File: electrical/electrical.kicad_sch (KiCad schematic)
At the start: 0 parts

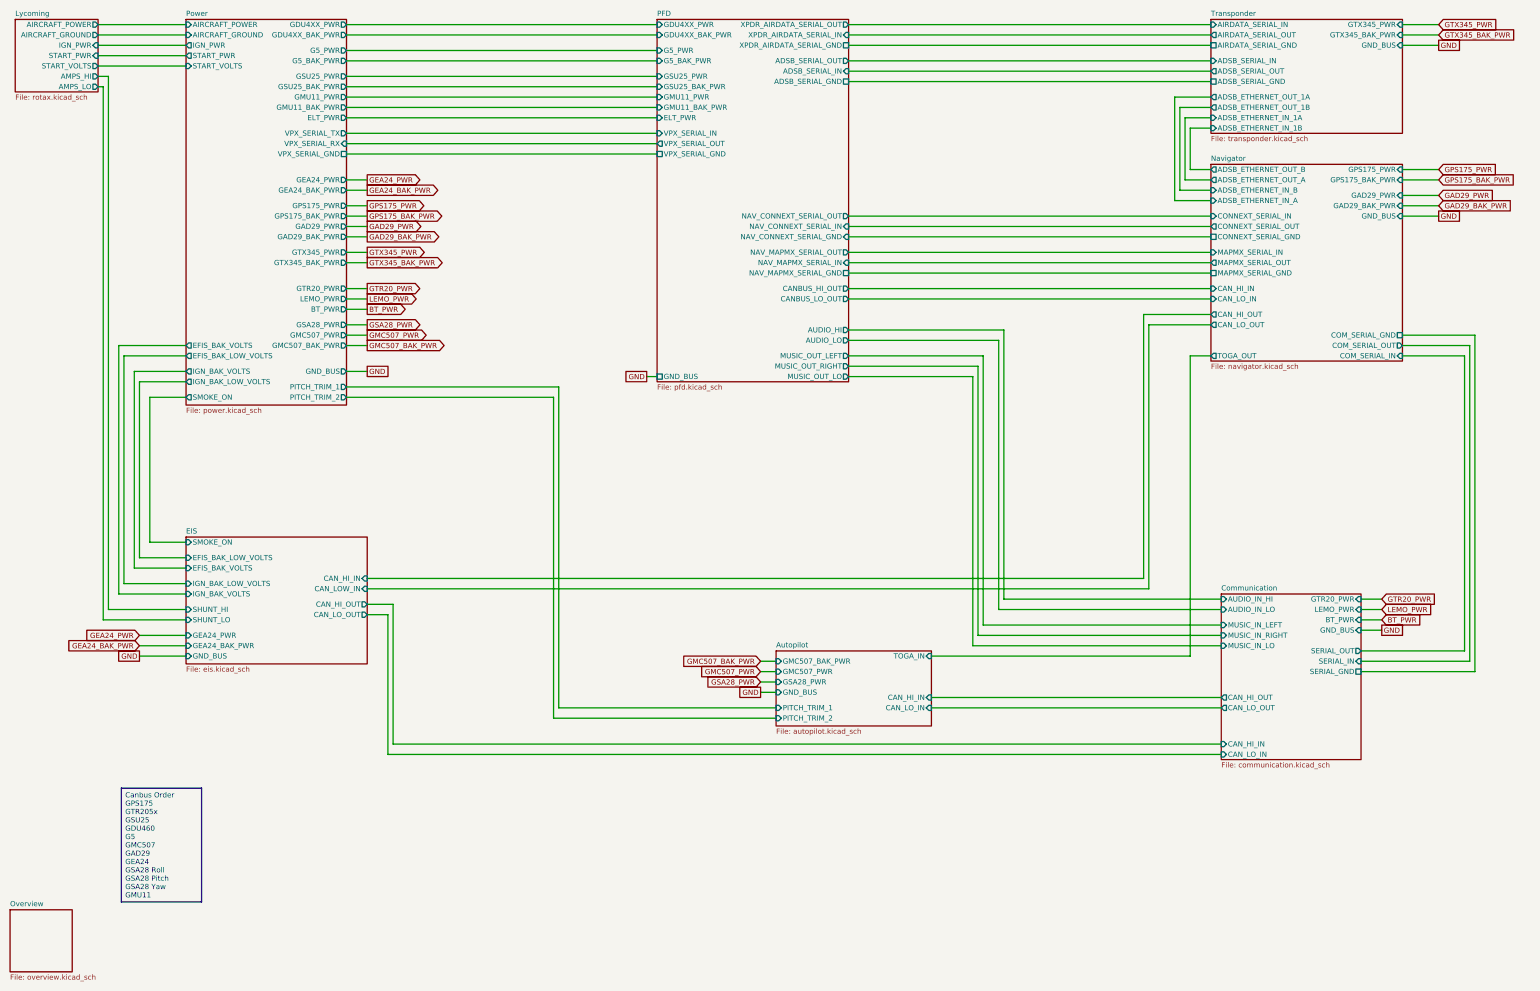
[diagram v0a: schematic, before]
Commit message: Changed GPS 175 to not have connection to GTS 205x per g3xpert. Moved ELT GPS from GPS 175 and used RS-232 on GDU 460 for GEA 24 backup.
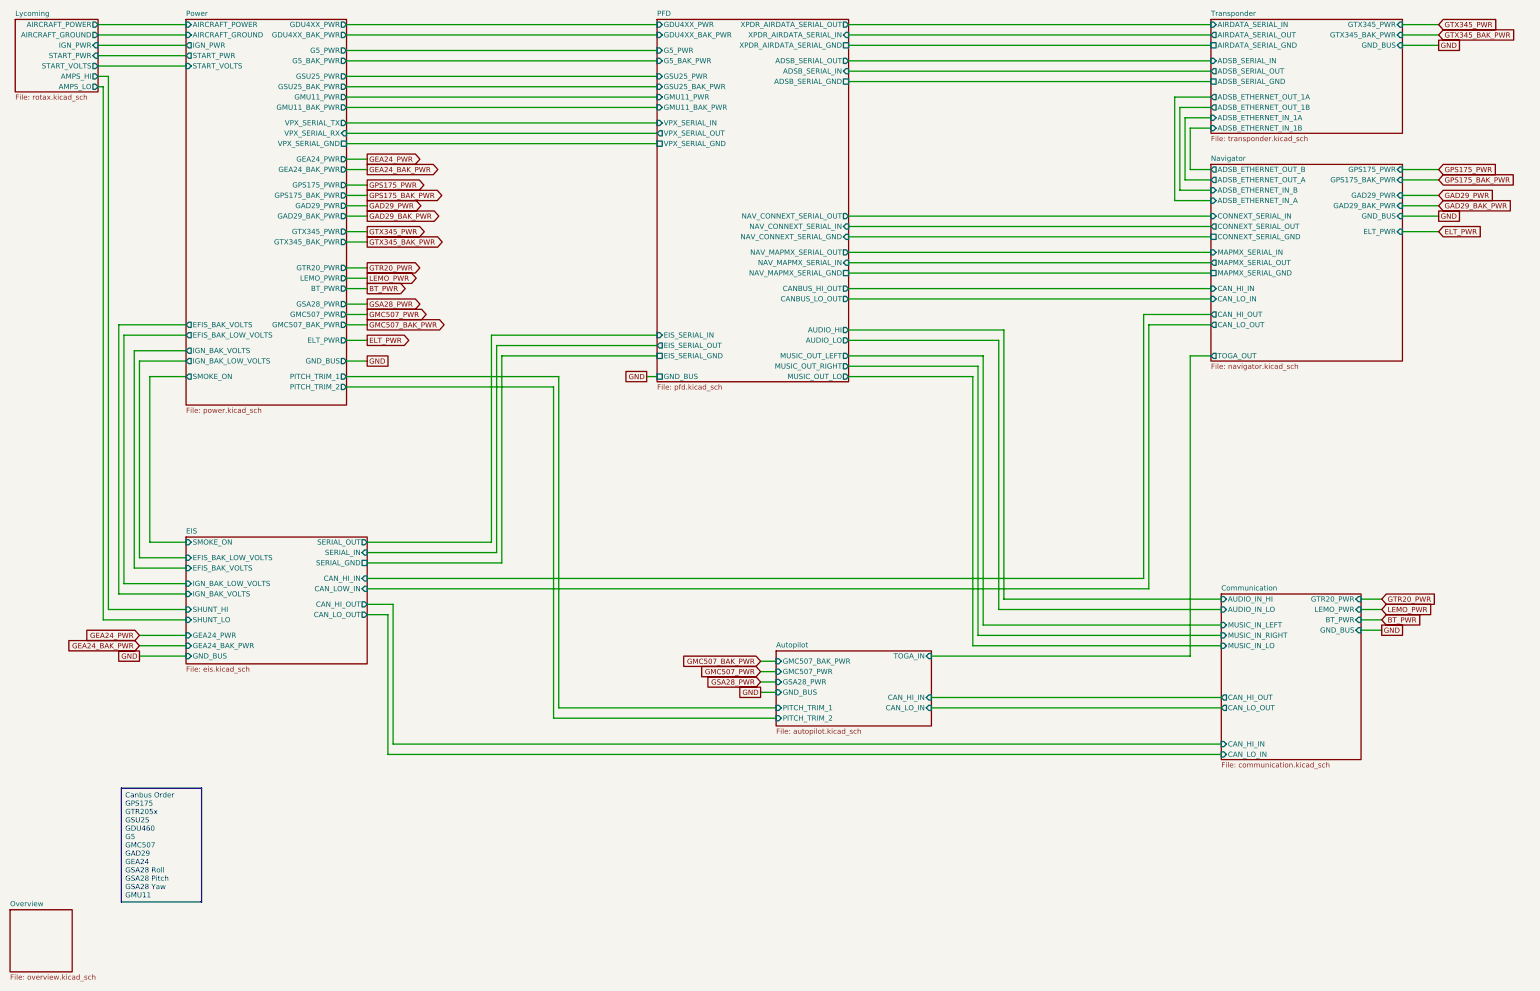
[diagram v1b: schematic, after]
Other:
- sheet Communication ports: added none; removed SERIAL_GND, SERIAL_IN, SERIAL_OUT
- sheet EIS ports: added SERIAL_GND, SERIAL_IN, SERIAL_OUT; removed none
- sheet Navigator ports: added ELT_PWR; removed COM_SERIAL_GND, COM_SERIAL_IN, COM_SERIAL_OUT
- sheet PFD ports: added EIS_SERIAL_GND, EIS_SERIAL_IN, EIS_SERIAL_OUT; removed ELT_PWR

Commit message: Rewired canbus to match physical order.
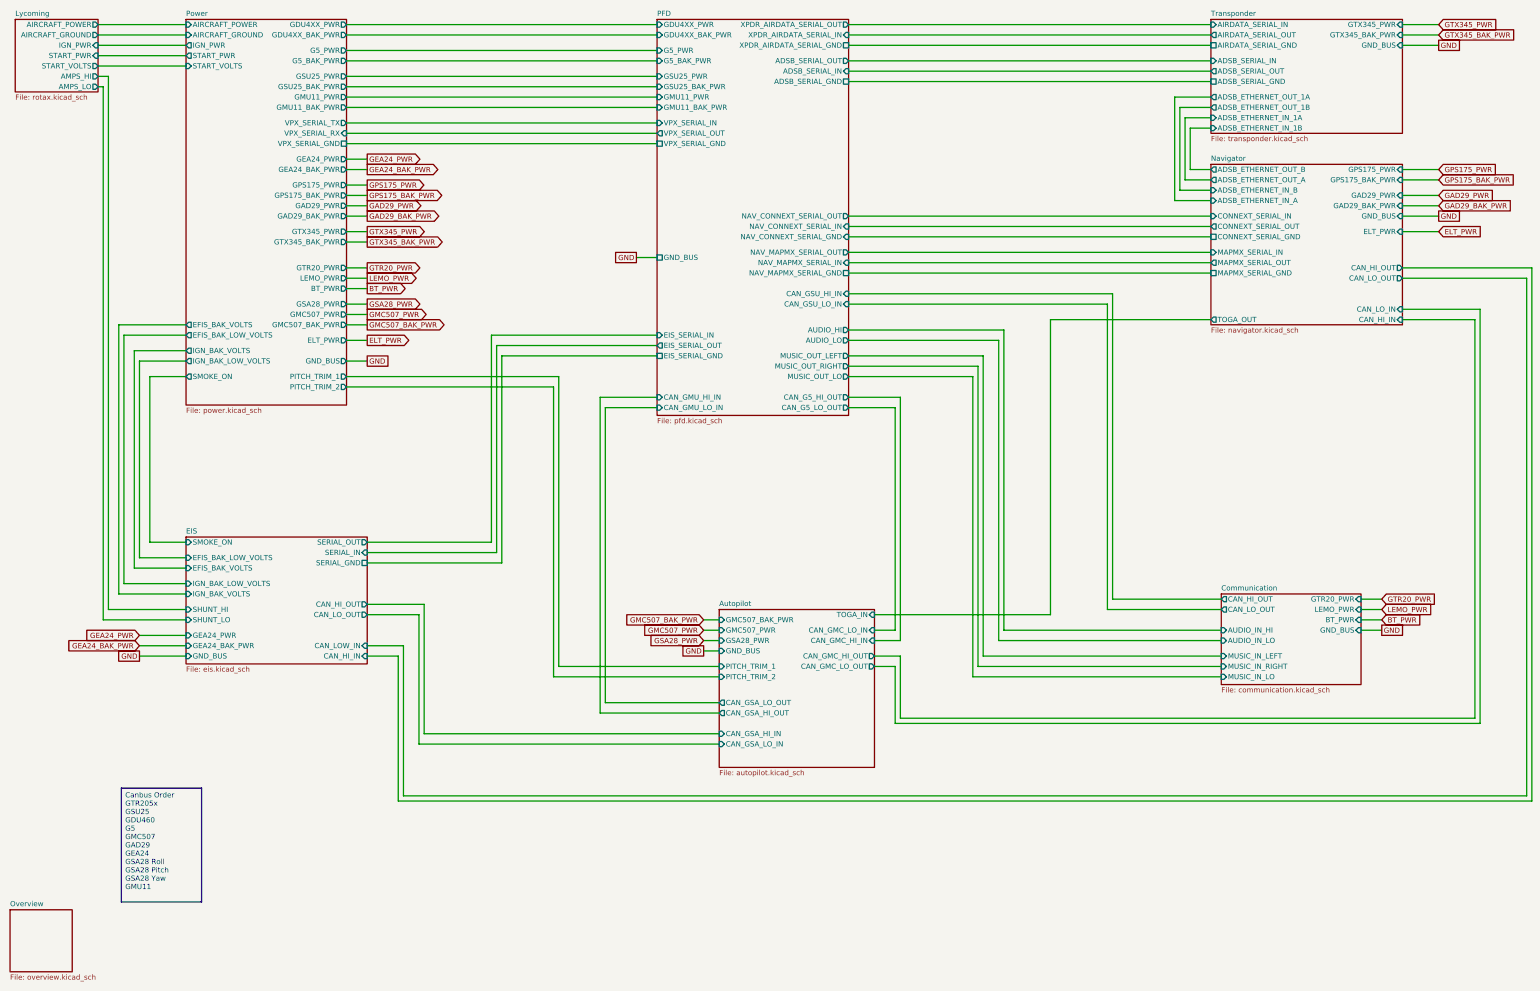
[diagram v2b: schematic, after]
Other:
- sheet Autopilot ports: added CAN_GMC_HI_IN, CAN_GMC_HI_OUT, CAN_GMC_LO_IN, CAN_GMC_LO_OUT, CAN_GSA_HI_IN, CAN_GSA_HI_OUT, CAN_GSA_LO_IN, CAN_GSA_LO_OUT; removed CAN_HI_IN, CAN_LO_IN
- sheet Communication ports: added none; removed CAN_HI_IN, CAN_LO_IN
- sheet PFD ports: added CAN_G5_HI_OUT, CAN_G5_LO_OUT, CAN_GMU_HI_IN, CAN_GMU_LO_IN, CAN_GSU_HI_IN, CAN_GSU_LO_IN; removed CANBUS_HI_OUT, CANBUS_LO_OUT

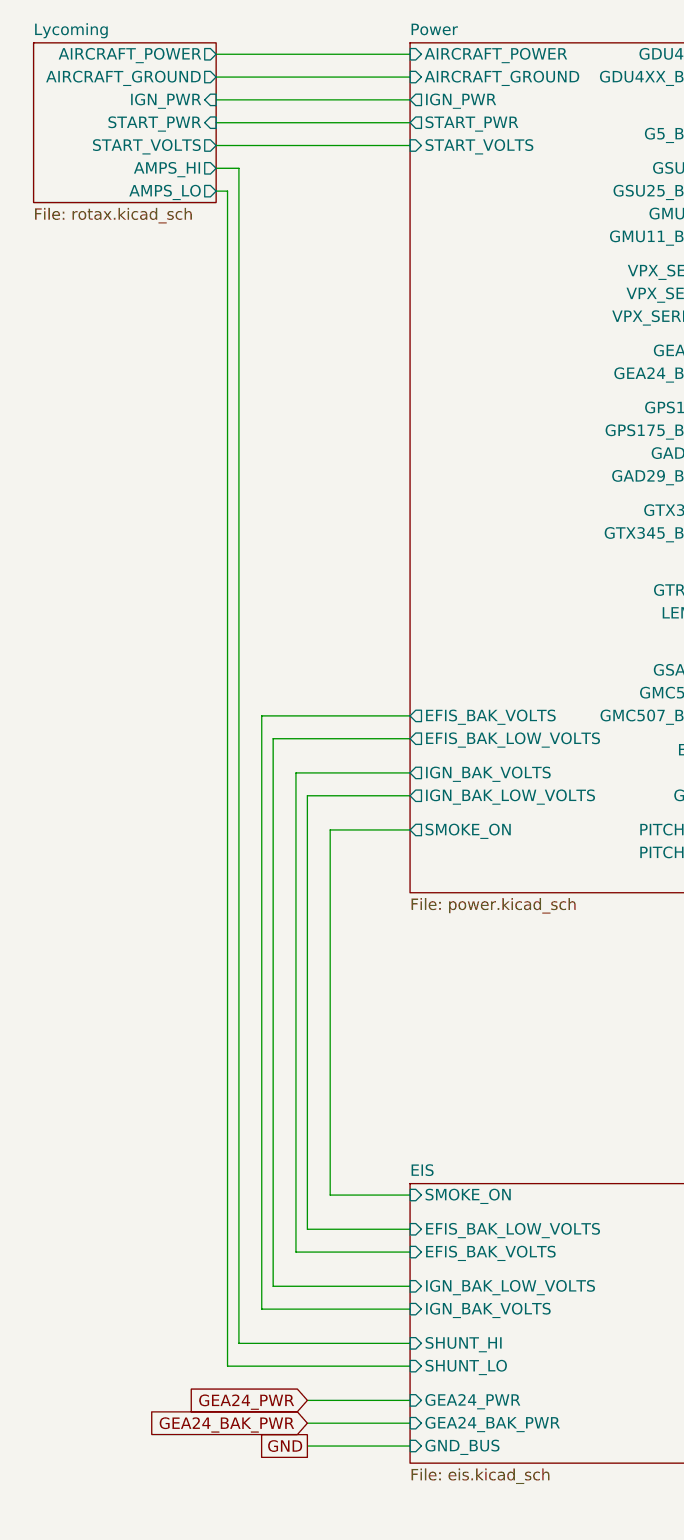
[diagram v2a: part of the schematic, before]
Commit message: Forgot to remove amps from overview.
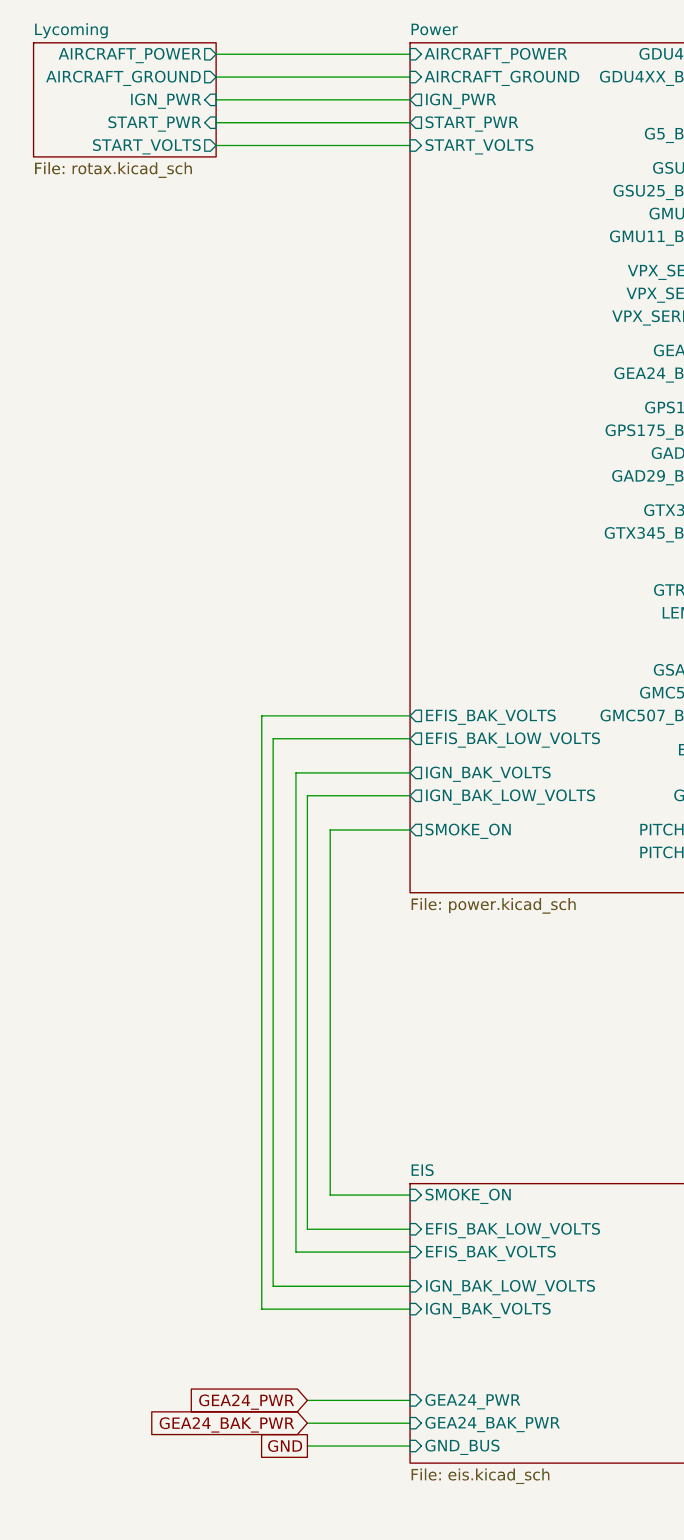
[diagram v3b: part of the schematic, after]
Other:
- sheet EIS ports: added none; removed SHUNT_HI, SHUNT_LO
- sheet Lycoming ports: added none; removed AMPS_HI, AMPS_LO
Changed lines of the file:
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@@
 	(title_block
 		(title "Electrical Overview")
-		(date "2025-09-09")
-		(rev "1.0.3")
+		(date "2025-09-29")
+		(rev "1.0.7")
 		(company "N78HR")
 	)
@@
 	(wire
 		(pts
-			(xy 38.1 45.72) (xy 38.1 176.53)
-		)
-		(stroke
-			(width 0)
-			(type default)
-		)
-	)
-	(wire
-		(pts
 			(xy 102.87 160.02) (xy 134.62 160.02)
 		)
@@
 	(wire
 		(pts
-			(xy 36.83 43.18) (xy 39.37 43.18)
-		)
-		(stroke
-			(width 0)
-			(type default)
-		)
-	)
-	(wire
-		(pts
 			(xy 133.35 157.48) (xy 133.35 106.68)
 		)
@@
 	(wire
 		(pts
-			(xy 38.1 176.53) (xy 58.42 176.53)
-		)
-		(stroke
-			(width 0)
-			(type default)
-		)
-	)
-	(wire
-		(pts
 			(xy 149.86 187.96) (xy 189.23 187.96)
 		)
@@
 	(wire
 		(pts
-			(xy 38.1 45.72) (xy 36.83 45.72)
-		)
-		(stroke
-			(width 0)
-			(type default)
-		)
-	)
-	(wire
-		(pts
 			(xy 102.87 172.72) (xy 116.84 172.72)
 		)
@@
 	(wire
 		(pts
-			(xy 39.37 173.99) (xy 58.42 173.99)
-		)
-		(stroke
-			(width 0)
-			(type default)
-		)
-	)
-	(wire
-		(pts
 			(xy 356.87 102.87) (xy 374.65 102.87)
 		)
@@
 	(wire
 		(pts
-			(xy 39.37 43.18) (xy 39.37 173.99)
-		)
-		(stroke
-			(width 0)
-			(type default)
-		)
-	)
-	(wire
-		(pts
 			(xy 375.92 100.33) (xy 356.87 100.33)
 		)
@@
 	(sheet
 		(at 16.51 29.21)
-		(size 20.32 17.78)
+		(size 20.32 12.7)
 		(exclude_from_sim no)
 		(in_bom yes)
@@
 		)
 		(property "Sheetfile" "rotax.kicad_sch"
-			(at 16.51 47.5746 0)
+			(at 16.51 42.4946 0)
 			(effects
 				(font
@@
 			)
 		)
-		(pin "AMPS_HI" output
-			(at 36.83 43.18 0)
-			(effects
-				(font
-					(size 1.27 1.27)
-				)
-				(justify right)
-			)
-		)
-		(pin "AMPS_LO" output
-			(at 36.83 45.72 0)
-			(effects
-				(font
-					(size 1.27 1.27)
-				)
-				(justify right)
-			)
-		)
 		(instances
 			(project "electrical"
@@
 			(effects
 				(font
-					(size 1.27 1.27)
-				)
-				(justify left)
-			)
-		)
-		(pin "SHUNT_HI" input
-			(at 58.42 173.99 180)
-			(effects
-				(font
-					(size 1.27 1.27)
-				)
-				(justify left)
-			)
-		)
-		(pin "SHUNT_LO" input
-			(at 58.42 176.53 180)
-			(effects
-				(font
